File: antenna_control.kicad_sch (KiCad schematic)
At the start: 26 parts, among them J7 G125-MH11005L1P, J9 FTSH-105-01-L-DV-K, Q12 DMP2160UWQ-7, Q13 DMP3056LDM-7, U46 M0L1228QRGERQ1

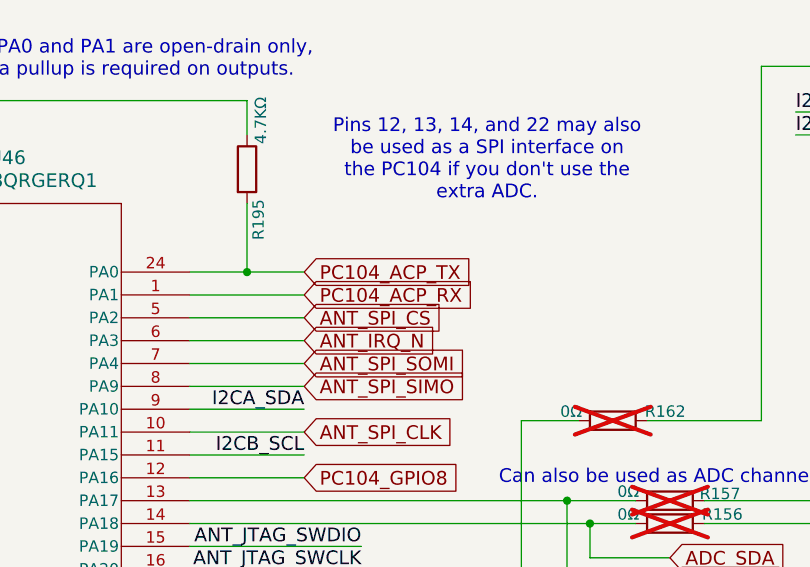
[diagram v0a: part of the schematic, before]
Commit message: Remove the serial connections from the PC104
The USB connection has proven itself, so it shouldn't be needed on later
boards.  This allowed some routing simplification.

Signed-off-by: Corey Minyard <corey@minyard.net>
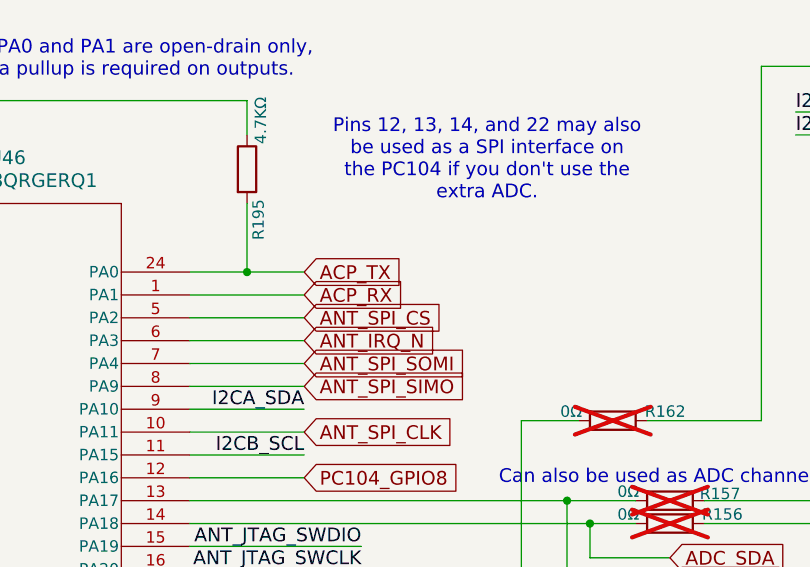
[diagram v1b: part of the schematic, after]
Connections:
- net PC104_ACP_RX renamed ACP_RX
- net PC104_ACP_TX renamed ACP_TX
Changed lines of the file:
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@@
 		)
 	)
-	(global_label "PC104_ACP_RX"
+	(global_label "ACP_RX"
 		(shape input)
 		(at 137.16 62.23 0)
@@
 		)
 	)
-	(global_label "PC104_ACP_TX"
+	(global_label "ACP_TX"
 		(shape input)
 		(at 137.16 59.69 0)

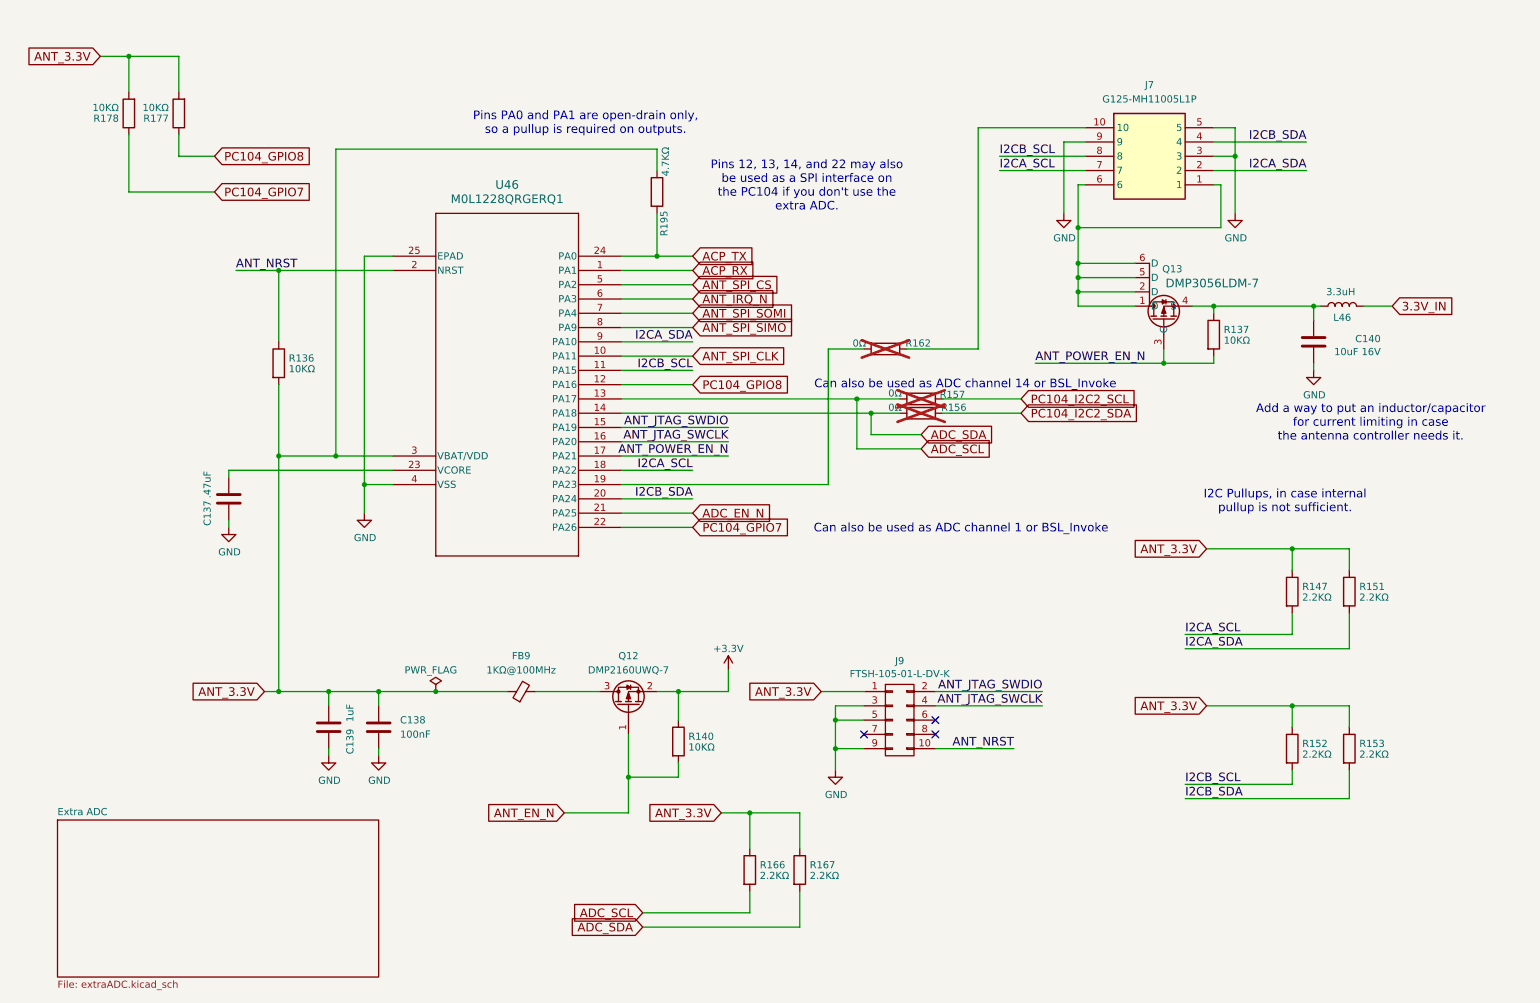
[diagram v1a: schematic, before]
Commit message: Tie the bootstrap load (BSL) lines into the USB chip
Through MOSFETs avoid CMOS latch up.  This will let GPIO lines on the
USB chip start the BSL process.

Signed-off-by: Corey Minyard <corey@minyard.net>
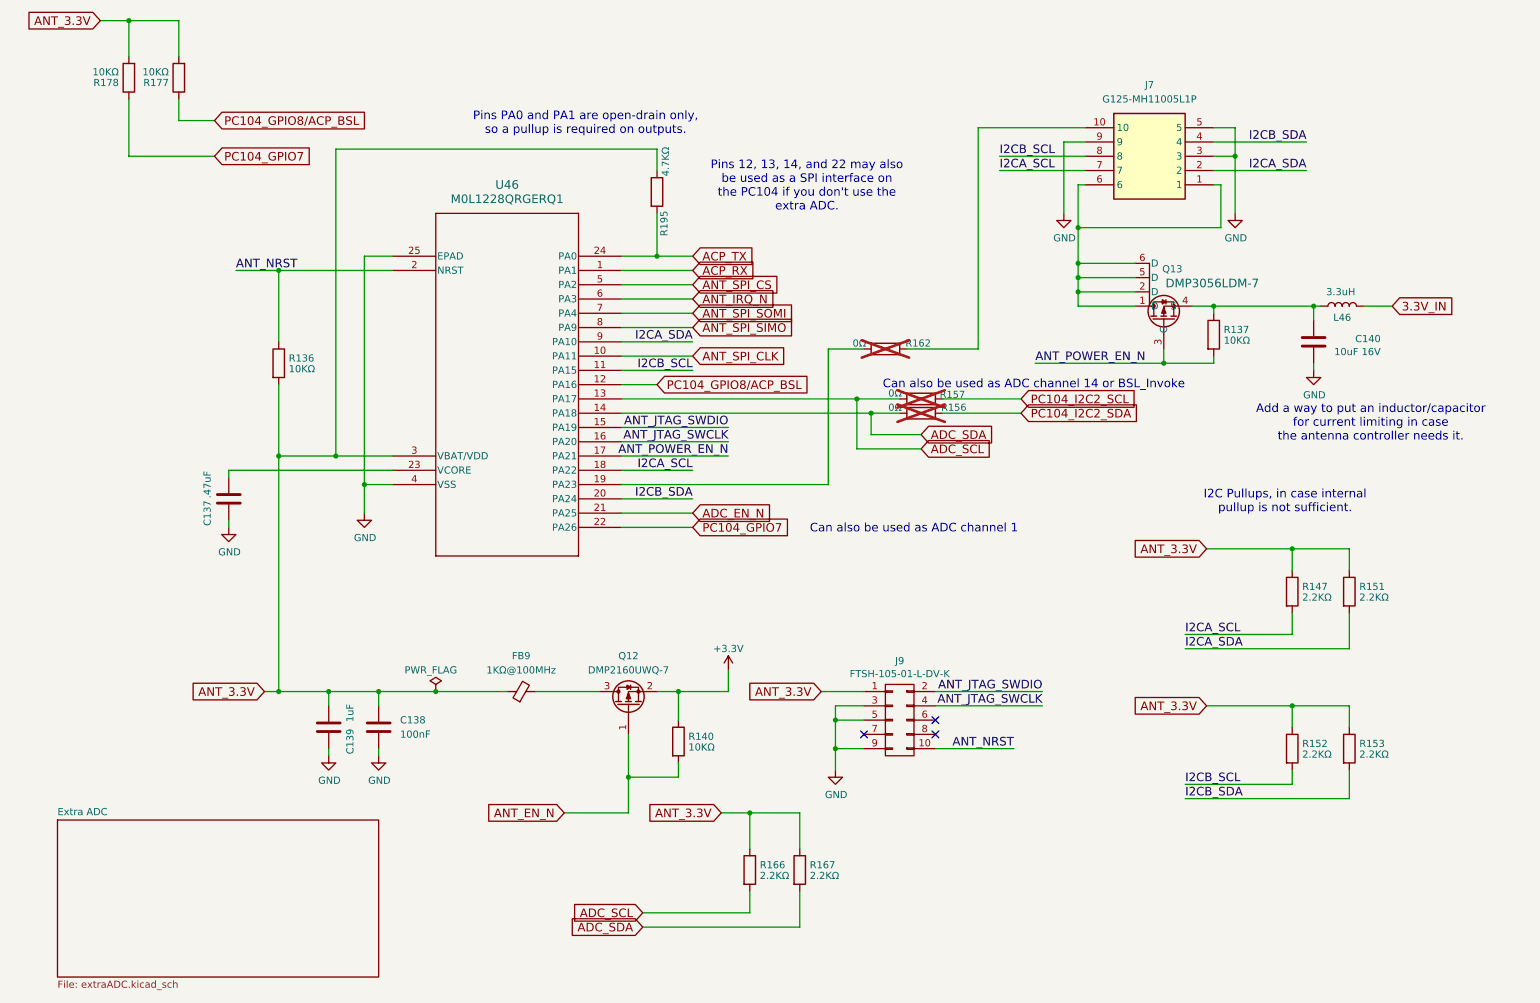
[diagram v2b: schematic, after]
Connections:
- net PC104_GPIO8 renamed PC104_GPIO8/ACP_BSL
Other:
- note added: "Can also be used as ADC channel 1"
- note removed: "Can also be used as ADC channel 1 or BSL_Invoke"
- moved on the sheet: R177, R178
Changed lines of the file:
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@@
 	(text "Can also be used as ADC channel 14 or BSL_Invoke"
 		(exclude_from_sim no)
-		(at 185.674 82.55 0)
+		(at 197.866 82.55 0)
 		(effects
 			(font
@@
 		)
 	)
-	(text "Can also be used as ADC channel 1 or BSL_Invoke"
+	(text "Can also be used as ADC channel 1"
 		(exclude_from_sim no)
-		(at 184.912 108.204 0)
+		(at 176.53 108.204 0)
 		(effects
 			(font
@@
 	)
 	(junction
-		(at 36.83 24.13)
+		(at 36.83 17.78)
 		(diameter 0)
 		(color 0 0 0 0)
@@
 	(wire
 		(pts
-			(xy 45.72 41.91) (xy 52.07 41.91)
+			(xy 45.72 35.56) (xy 52.07 35.56)
 		)
 		(stroke
@@
 	(wire
 		(pts
-			(xy 36.83 38.1) (xy 36.83 48.26)
+			(xy 36.83 31.75) (xy 36.83 41.91)
 		)
 		(stroke
@@
 	(wire
 		(pts
-			(xy 36.83 24.13) (xy 45.72 24.13)
+			(xy 36.83 17.78) (xy 45.72 17.78)
 		)
 		(stroke
@@
 	(wire
 		(pts
-			(xy 36.83 48.26) (xy 52.07 48.26)
+			(xy 36.83 41.91) (xy 52.07 41.91)
 		)
 		(stroke
@@
 	(wire
 		(pts
-			(xy 45.72 38.1) (xy 45.72 41.91)
+			(xy 45.72 31.75) (xy 45.72 35.56)
 		)
 		(stroke
@@
 	(wire
 		(pts
-			(xy 124.46 82.55) (xy 137.16 82.55)
+			(xy 124.46 82.55) (xy 130.81 82.55)
 		)
 		(stroke
@@
 	(wire
 		(pts
-			(xy 31.75 24.13) (xy 36.83 24.13)
+			(xy 31.75 17.78) (xy 36.83 17.78)
 		)
 		(stroke
@@
 	(wire
 		(pts
-			(xy 36.83 24.13) (xy 36.83 30.48)
+			(xy 36.83 17.78) (xy 36.83 24.13)
 		)
 		(stroke
@@
 	(wire
 		(pts
-			(xy 45.72 24.13) (xy 45.72 30.48)
+			(xy 45.72 17.78) (xy 45.72 24.13)
 		)
 		(stroke
@@
 		)
 	)
-	(global_label "PC104_GPIO8"
+	(global_label "PC104_GPIO8{slash}ACP_BSL"
 		(shape input)
-		(at 137.16 82.55 0)
+		(at 130.81 82.55 0)
 		(fields_autoplaced yes)
 		(effects
@@
 		)
 		(property "Intersheetrefs" "${INTERSHEET_REFS}"
-			(at 155.3418 82.55 0)
+			(at 160.3129 82.55 0)
 			(effects
 				(font
@@
 	(global_label "ANT_3.3V"
 		(shape input)
-		(at 31.75 24.13 180)
+		(at 31.75 17.78 180)
 		(fields_autoplaced yes)
 		(effects
@@
 		)
 		(property "Intersheetrefs" "${INTERSHEET_REFS}"
-			(at 18.7933 24.13 0)
+			(at 18.7933 17.78 0)
 			(effects
 				(font
@@
 	(global_label "PC104_GPIO7"
 		(shape input)
-		(at 52.07 48.26 0)
+		(at 52.07 41.91 0)
 		(fields_autoplaced yes)
 		(effects
@@
 		)
 		(property "Intersheetrefs" "${INTERSHEET_REFS}"
-			(at 70.2518 48.26 0)
+			(at 70.2518 41.91 0)
 			(effects
 				(font
@@
 		)
 	)
-	(global_label "PC104_GPIO8"
+	(global_label "PC104_GPIO8{slash}ACP_BSL"
 		(shape input)
-		(at 52.07 41.91 0)
+		(at 52.07 35.56 0)
 		(fields_autoplaced yes)
 		(effects
@@
 		)
 		(property "Intersheetrefs" "${INTERSHEET_REFS}"
-			(at 70.2518 41.91 0)
+			(at 81.5729 35.56 0)
 			(effects
 				(font
@@
 	(symbol
 		(lib_id "Device:R")
-		(at 45.72 34.29 180)
+		(at 45.72 27.94 180)
 		(unit 1)
 		(exclude_from_sim no)
@@
 		(dnp no)
 		(property "Reference" "R177"
-			(at 43.942 35.179 0)
+			(at 43.942 28.829 0)
 			(effects
 				(font
@@
 		)
 		(property "Value" "10KΩ"
-			(at 43.942 33.274 0)
+			(at 43.942 26.924 0)
 			(effects
 				(font
@@
 		)
 		(property "Footprint" "Resistor_SMD:R_0402_1005Metric_Pad0.72x0.64mm_HandSolder"
-			(at 47.498 34.29 90)
+			(at 47.498 27.94 90)
 			(effects
 				(font
@@
 		)
 		(property "Datasheet" "~"
-			(at 45.72 34.29 0)
+			(at 45.72 27.94 0)
 			(effects
 				(font
@@
 		)
 		(property "Description" ""
-			(at 45.72 34.29 0)
+			(at 45.72 27.94 0)
 			(effects
 				(font
@@
 	(symbol
 		(lib_id "Device:R")
-		(at 36.83 34.29 180)
+		(at 36.83 27.94 180)
 		(unit 1)
 		(exclude_from_sim no)
@@
 		(dnp no)
 		(property "Reference" "R178"
-			(at 35.052 35.179 0)
+			(at 35.052 28.829 0)
 			(effects
 				(font
@@
 		)
 		(property "Value" "10KΩ"
-			(at 35.052 33.274 0)
+			(at 35.052 26.924 0)
 			(effects
 				(font
@@
 		)
 		(property "Footprint" "Resistor_SMD:R_0402_1005Metric_Pad0.72x0.64mm_HandSolder"
-			(at 38.608 34.29 90)
+			(at 38.608 27.94 90)
 			(effects
 				(font
@@
 		)
 		(property "Datasheet" "~"
-			(at 36.83 34.29 0)
+			(at 36.83 27.94 0)
 			(effects
 				(font
@@
 		)
 		(property "Description" ""
-			(at 36.83 34.29 0)
+			(at 36.83 27.94 0)
 			(effects
 				(font
